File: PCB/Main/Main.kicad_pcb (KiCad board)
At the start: 2 copper layers, 2 parts, among them J1 PICO LEFT, J2 PICO Right

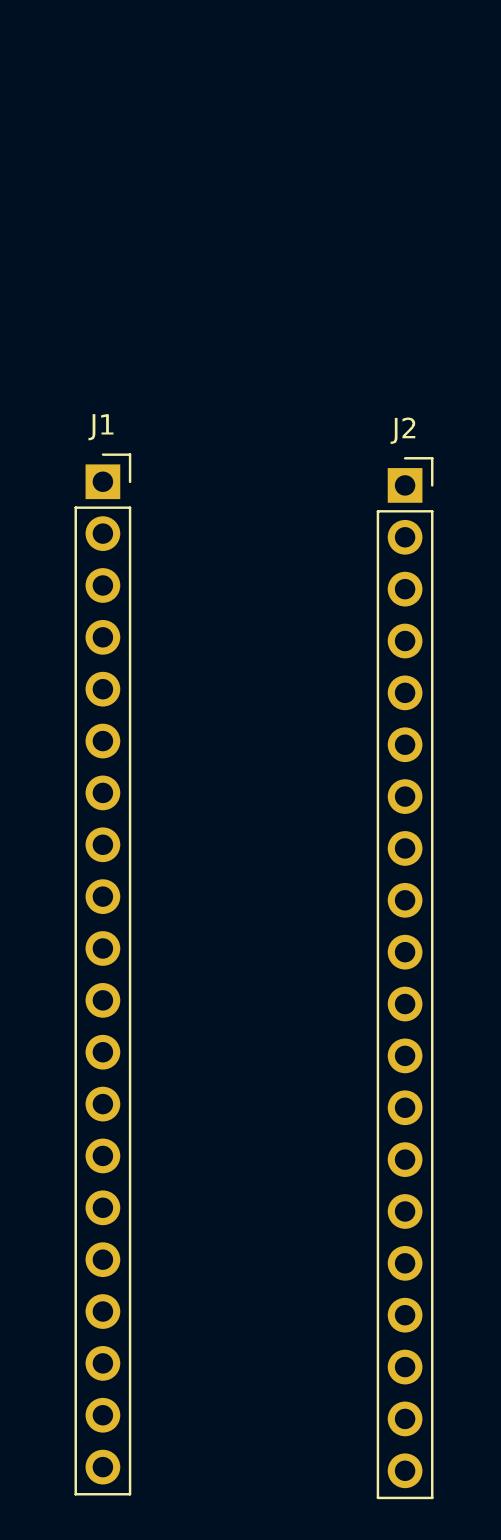
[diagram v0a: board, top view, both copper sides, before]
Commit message: PCB editing
changes to footprints.
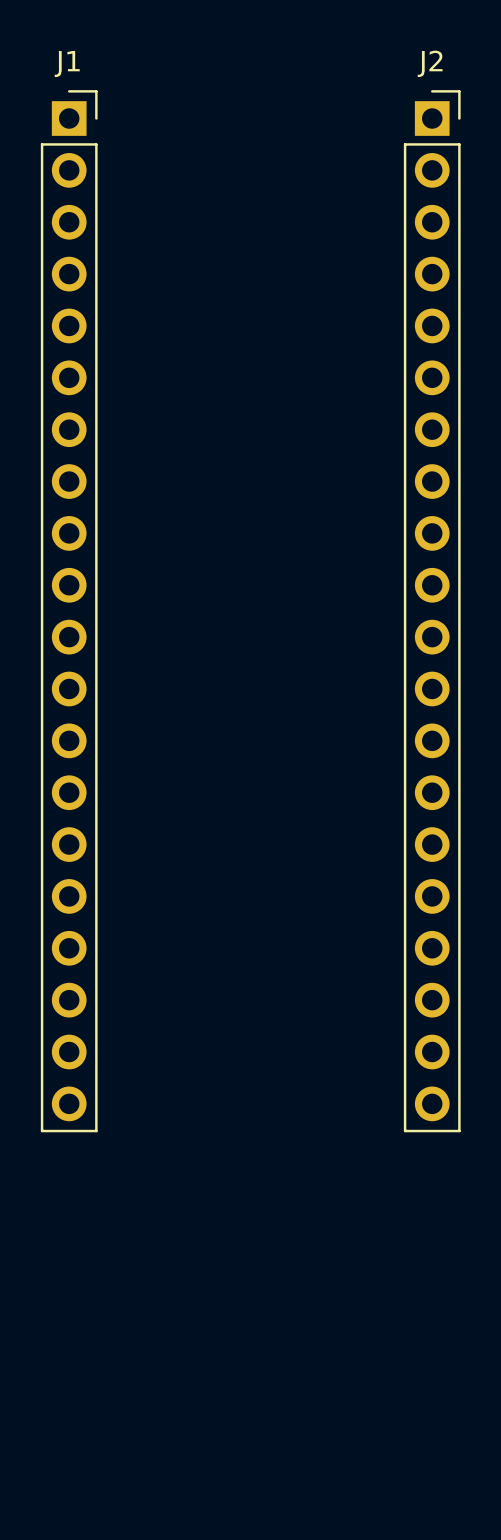
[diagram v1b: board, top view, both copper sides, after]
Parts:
- moved J2 18.0 mm to (117.8, 50.0)
- moved J1 17.9 mm to (100.0, 50.0)
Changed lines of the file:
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@@
 	(footprint "Connector_PinSocket_2.54mm:PinSocket_1x20_P2.54mm_Vertical"
 		(layer "F.Cu")
-		(at 101.7 67.74)
+		(at 100.05 49.95)
 		(descr "Through hole straight socket strip, 1x20, 2.54mm pitch, single row (from Kicad 4.0.7), script generated")
 		(tags "Through hole socket strip THT 1x20 2.54mm single row")
@@
 	(footprint "Connector_PinSocket_2.54mm:PinSocket_1x20_P2.54mm_Vertical"
 		(layer "F.Cu")
-		(at 116.5 67.92)
+		(at 117.83 49.95)
 		(descr "Through hole straight socket strip, 1x20, 2.54mm pitch, single row (from Kicad 4.0.7), script generated")
 		(tags "Through hole socket strip THT 1x20 2.54mm single row")

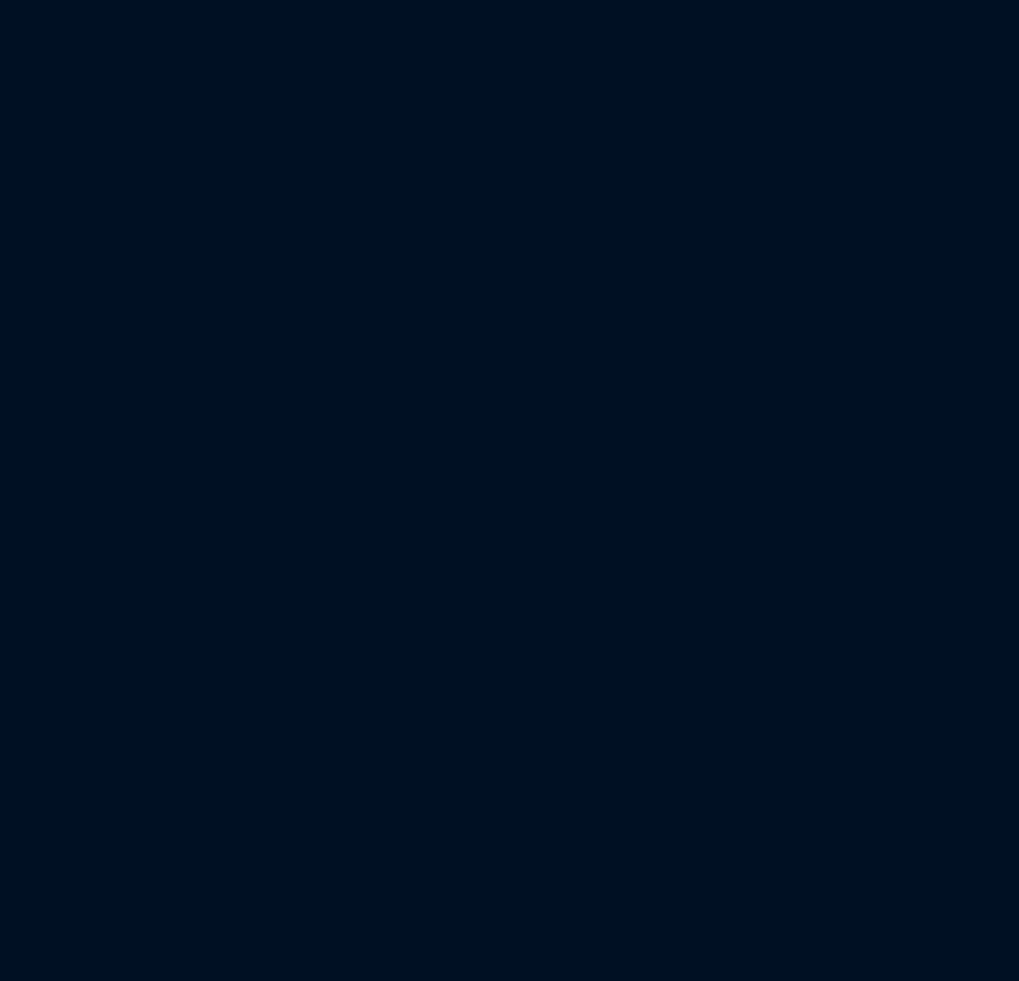
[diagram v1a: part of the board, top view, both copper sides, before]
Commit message: PLACED TB6612FNG Motor driver on schematic.
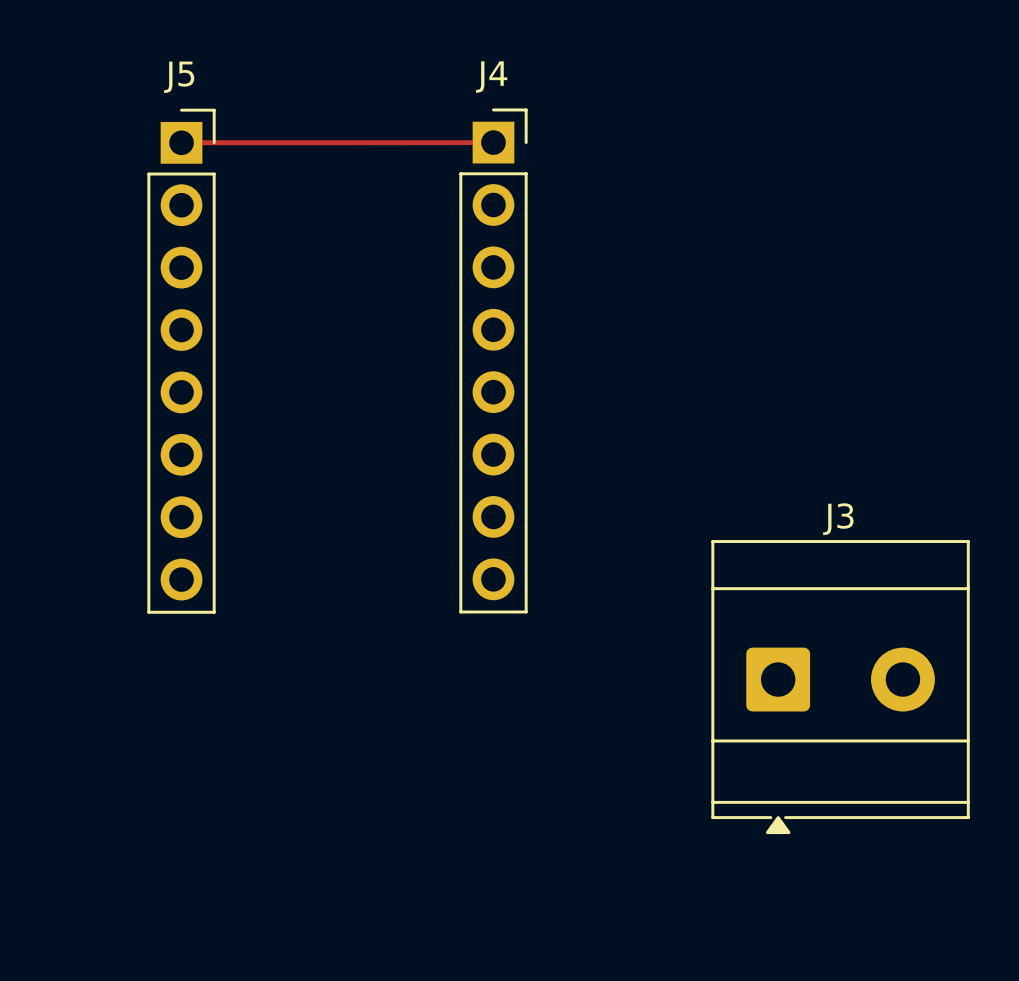
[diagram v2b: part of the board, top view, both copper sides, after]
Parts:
- added J3: Screw_Terminal_01x02, TerminalBlock_MetzConnect:TerminalBlock_MetzConnect_Type073_RT02602HBLU_1x02_P5.08mm_Horizontal, F.Cu at (231.3, 71.8)
- added J4: TB6612FNG_right, Connector_PinSocket_2.54mm:PinSocket_1x08_P2.54mm_Vertical, F.Cu at (219.7, 49.9)
- added J5: TB6612FNG_left, Connector_PinSocket_2.54mm:PinSocket_1x08_P2.54mm_Vertical, F.Cu at (207.0, 49.9)
